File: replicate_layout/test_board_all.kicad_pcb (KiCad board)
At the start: 2 copper layers, 30 parts, among them J1001 Pusa_4mm, J1002 Pusa_4mm, Q1001 CSD19531KCS, Q1002 CSD19531KCS, Q1003 CSD19531KCS, Q2001 CSD19531KCS, Q2002 CSD19531KCS, Q3001 CSD19531KCS, Q3002 CSD19531KCS, Q4001 CSD19531KCS, Q4002 CSD19531KCS, U1001 LAUNCHXL-F28377S, U2001 IR2181, U3001 IR2181, U4001 IR2181

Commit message: polarna replikacija dela GUI še ne dela samo še zone je treba replicirati
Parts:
- moved Q1001 147.0 mm to (40.6, 167.6)
- moved Q1002 147.0 mm to (29.8, 175.3)
- moved Q1003 147.0 mm to (29.2, 188.6)
- moved U1001 61.4 mm to (19.7, 48.9)
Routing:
- net /Veja_3/OUT: track 63.8 -> 44.0 mm
- removed copper zone on F.Cu, net /Veja_1/OUT
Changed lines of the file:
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@@
     (thickness 1.6)
     (drawings 0)
-    (tracks 149)
+    (tracks 146)
     (zones 0)
     (modules 30)
@@
     (tags "capacitor 1206")
     (attr smd)
-    (fp_text reference C2001 (at 0 -1.75) (layer F.SilkS)
+    (fp_text reference C2001 (at 4.675 0) (layer F.SilkS)
       (effects (font (size 1 1) (thickness 0.15)))
     )
@@
     (tags "capacitor 1206")
     (attr smd)
-    (fp_text reference C3001 (at 0 -1.75) (layer F.SilkS)
+    (fp_text reference C3001 (at 4.675 0) (layer F.SilkS)
       (effects (font (size 1 1) (thickness 0.15)))
     )
@@
     (tags "capacitor 1206")
     (attr smd)
-    (fp_text reference C4001 (at 0 -1.75) (layer F.SilkS)
+    (fp_text reference C4001 (at 4.675 0) (layer F.SilkS)
       (effects (font (size 1 1) (thickness 0.15)))
     )
@@
     (tags "Diode Mini-MELF")
     (attr smd)
-    (fp_text reference D2001 (at 0 -2 270) (layer F.SilkS)
+    (fp_text reference D2001 (at 0 1.905 270) (layer F.SilkS)
       (effects (font (size 1 1) (thickness 0.15)))
     )
@@
       (effects (font (size 1 1) (thickness 0.15)))
     )
-    (fp_text user %R (at 0 -2 270) (layer F.Fab)
+    (fp_text user %R (at 0 1.905 270) (layer F.Fab)
       (effects (font (size 1 1) (thickness 0.15)))
     )
@@
     (tags "Diode Mini-MELF")
     (attr smd)
-    (fp_text reference D3001 (at 0 -2 270) (layer F.SilkS)
+    (fp_text reference D3001 (at 0 1.905 270) (layer F.SilkS)
       (effects (font (size 1 1) (thickness 0.15)))
     )
@@
       (effects (font (size 1 1) (thickness 0.15)))
     )
-    (fp_text user %R (at 0 -2 270) (layer F.Fab)
+    (fp_text user %R (at 0 1.905 270) (layer F.Fab)
       (effects (font (size 1 1) (thickness 0.15)))
     )
@@
     (tags "Diode Mini-MELF")
     (attr smd)
-    (fp_text reference D4001 (at 0 -2 270) (layer F.SilkS)
+    (fp_text reference D4001 (at 0 1.905 270) (layer F.SilkS)
       (effects (font (size 1 1) (thickness 0.15)))
     )
@@
       (effects (font (size 1 1) (thickness 0.15)))
     )
-    (fp_text user %R (at 0 -2 270) (layer F.Fab)
+    (fp_text user %R (at 0 1.905 270) (layer F.Fab)
       (effects (font (size 1 1) (thickness 0.15)))
     )
@@
   )
   (module Discretes:TO-220 (layer F.Cu)
-    (at 182.245 128.27)
+    (at 40.64 167.64)
     (descr "TO-220-3, Vertical, RM 2.54mm")
     (tags "TO-220-3 Vertical RM 2.54mm")
@@
   )
   (module Discretes:TO-220 (layer F.Cu)
-    (at 171.45 135.89)
+    (at 29.845 175.26)
     (descr "TO-220-3, Vertical, RM 2.54mm")
     (tags "TO-220-3 Vertical RM 2.54mm")
@@
   )
   (module Discretes:TO-220 (layer F.Cu)
-    (at 170.815 149.225)
+    (at 29.21 188.595)
     (descr "TO-220-3, Vertical, RM 2.54mm")
     (tags "TO-220-3 Vertical RM 2.54mm")
@@
   )
   (module TI_modules:28379D_launchpad (layer F.Cu)
-    (at 75.565 74.295 270)
+    (at 19.685 48.895 270)
     (descr "28379D launchpad")
     (tags DEV)
@@
     (tags "SOIC 1.27")
     (attr smd)
-    (fp_text reference U2001 (at 0 -3.5 90) (layer F.SilkS)
+    (fp_text reference U2001 (at -5.08 -3.81 90) (layer F.SilkS)
       (effects (font (size 1 1) (thickness 0.15)))
     )
@@
     (tags "SOIC 1.27")
     (attr smd)
-    (fp_text reference U3001 (at 0 -3.5 90) (layer F.SilkS)
+    (fp_text reference U3001 (at -5.08 -3.81 90) (layer F.SilkS)
       (effects (font (size 1 1) (thickness 0.15)))
     )
@@
     (tags "SOIC 1.27")
     (attr smd)
-    (fp_text reference U4001 (at 0 -3.5 90) (layer F.SilkS)
+    (fp_text reference U4001 (at -5.08 -3.81 90) (layer F.SilkS)
       (effects (font (size 1 1) (thickness 0.15)))
     )
@@
   (segment (start 200.66 106.235) (end 201.105 106.68) (width 0.5) (layer F.Cu) (net 1))
   (segment (start 200.66 102.715) (end 200.66 106.235) (width 0.5) (layer F.Cu) (net 1))
-  (segment (start 229.87 91.44) (end 229.87 92.075) (width 2) (layer F.Cu) (net 13))
-  (segment (start 234.95 86.36) (end 229.87 91.44) (width 2) (layer F.Cu) (net 13))
-  (segment (start 247.015 86.36) (end 234.95 86.36) (width 2) (layer F.Cu) (net 13))
   (segment (start 177.8 102.715) (end 177.8 106.235) (width 0.5) (layer F.Cu) (net 1))
   (segment (start 177.8 106.235) (end 178.245 106.68) (width 0.5) (layer F.Cu) (net 1))
@@
   (segment (start 186.69 101.29) (end 184.315 103.665) (width 0.5) (layer F.Cu) (net 25))
   (segment (start 184.315 103.665) (end 183.515 103.665) (width 0.5) (layer F.Cu) (net 25))
-  (zone (net 3) (net_name /Veja_1/OUT) (layer F.Cu) (hatch edge 0.508)
+  (zone (net 4) (net_name /Veja_2/OUT) (layer F.Cu) (hatch edge 0.508)
     (connect_pads (clearance 0.508))
     (min_thickness 0.254)
-    (fill yes (arc_segments 16) (thermal_gap 0.508) (thermal_bridge_width 0.508))
+    (fill (arc_segments 16) (thermal_gap 0.508) (thermal_bridge_width 0.508))
     (polygon
       (pts
-        (xy 181.61 86.995) (xy 184.15 86.995) (xy 184.15 93.345) (xy 181.61 93.345)
+        (xy 204.47 86.995) (xy 207.01 86.995) (xy 207.01 93.345) (xy 204.47 93.345)
       )
     )
@@
       )
     )
-  )
-  (zone (net 4) (net_name /Veja_2/OUT) (layer F.Cu) (hatch edge 0.508)
-    (connect_pads (clearance 0.508))
-    (min_thickness 0.254)
-    (fill (arc_segments 16) (thermal_gap 0.508) (thermal_bridge_width 0.508))
-    (polygon
-      (pts
-        (xy 204.47 86.995) (xy 207.01 86.995) (xy 207.01 93.345) (xy 204.47 93.345)
-      )
-    )
-  )
-  (zone (net 2) (net_name GND) (layer F.Cu) (hatch edge 0.508)
-    (connect_pads (clearance 0.508))
-    (min_thickness 0.254)
-    (fill yes (arc_segments 16) (thermal_gap 0.508) (thermal_bridge_width 0.508))
-    (polygon
-      (pts
-        (xy 188.595 92.075) (xy 188.595 90.17) (xy 191.77 90.17) (xy 191.77 92.075)
-      )
-    )
-  )
-  (zone (net 3) (net_name /Veja_1/OUT) (layer F.Cu) (hatch edge 0.508)
-    (connect_pads (clearance 0.508))
-    (min_thickness 0.254)
-    (fill yes (arc_segments 16) (thermal_gap 0.508) (thermal_bridge_width 0.508))
-    (polygon
-      (pts
-        (xy 182.88 77.47) (xy 182.88 85.09) (xy 191.135 85.09) (xy 191.135 77.47)
-      )
-    )

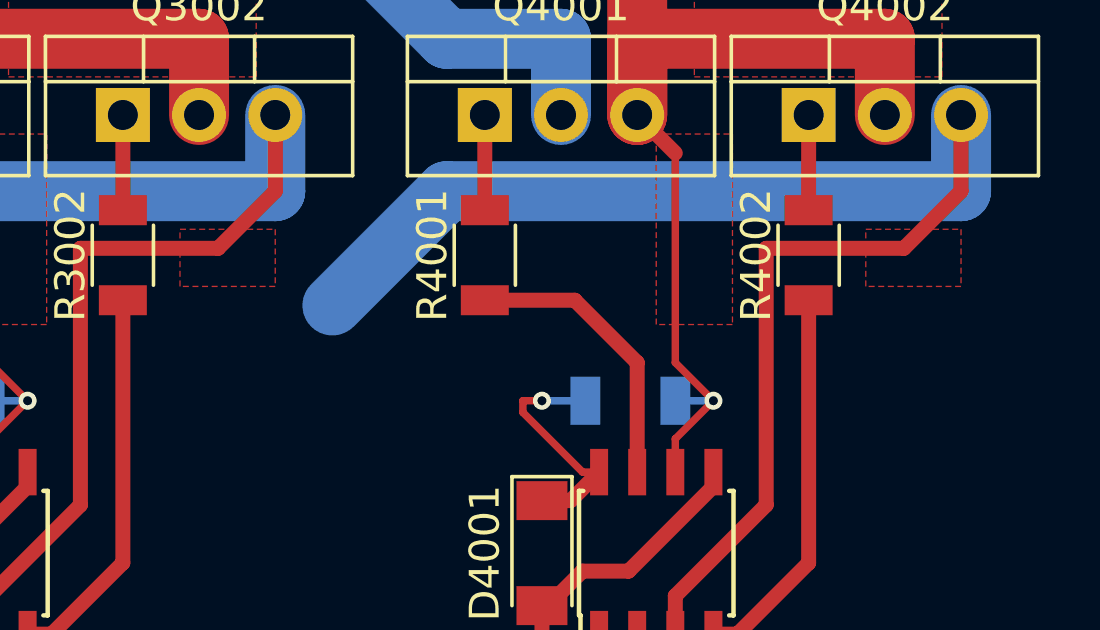
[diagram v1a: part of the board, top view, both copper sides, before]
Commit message: fixed a bug in test function changed how bounding box is calculated
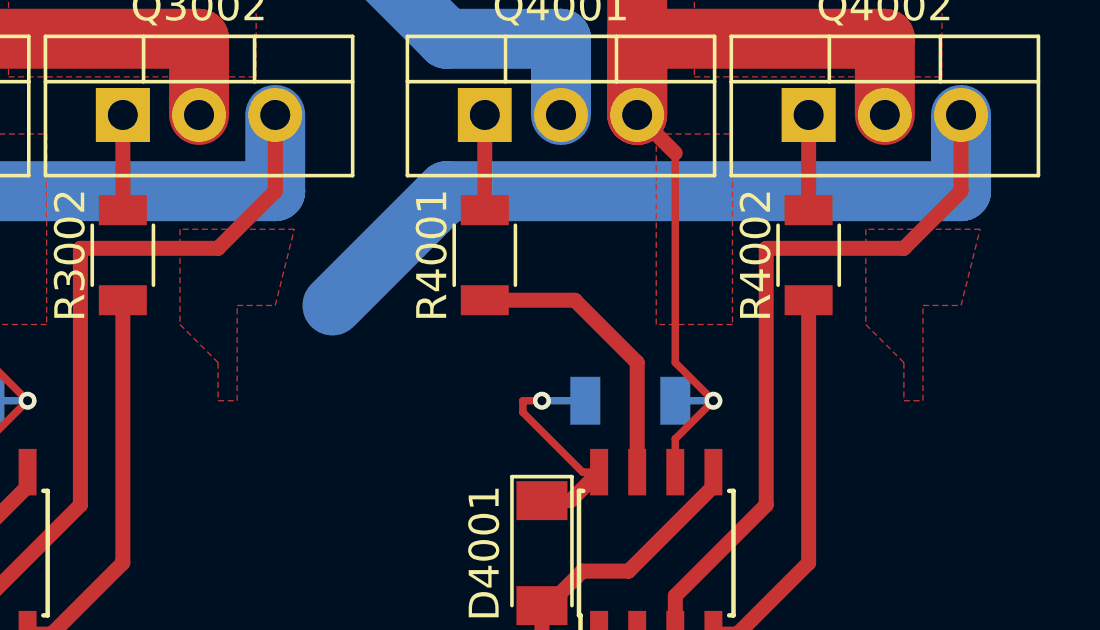
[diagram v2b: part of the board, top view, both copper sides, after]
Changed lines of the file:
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@@
+    )
+  )
+  (zone (net 2) (net_name GND) (layer F.Cu) (hatch edge 0.508)
+    (connect_pads (clearance 0.508))
+    (min_thickness 0.254)
+    (fill (arc_segments 16) (thermal_gap 0.508) (thermal_bridge_width 0.508))
+    (polygon
+      (pts
+        (xy 234.315 90.17) (xy 234.315 93.345) (xy 235.585 94.615) (xy 235.585 95.885) (xy 236.22 95.885)
+        (xy 236.22 92.71) (xy 237.49 92.71) (xy 238.125 90.17)
+      )
     )
   )
@@
       (pts
         (xy 228.6 77.47) (xy 228.6 85.09) (xy 236.855 85.09) (xy 236.855 77.47)
-      )
-    )
-  )
-  (zone (net 2) (net_name GND) (layer F.Cu) (hatch edge 0.508)
-    (connect_pads (clearance 0.508))
-    (min_thickness 0.254)
-    (fill (arc_segments 16) (thermal_gap 0.508) (thermal_bridge_width 0.508))
-    (polygon
-      (pts
-        (xy 234.315 92.075) (xy 234.315 90.17) (xy 237.49 90.17) (xy 237.49 92.075)
       )
     )
@@
     )
   )
+  (zone (net 2) (net_name GND) (layer F.Cu) (hatch edge 0.508)
+    (connect_pads (clearance 0.508))
+    (min_thickness 0.254)
+    (fill (arc_segments 16) (thermal_gap 0.508) (thermal_bridge_width 0.508))
+    (polygon
+      (pts
+        (xy 211.455 90.17) (xy 211.455 93.345) (xy 212.725 94.615) (xy 212.725 95.885) (xy 213.36 95.885)
+        (xy 213.36 92.71) (xy 214.63 92.71) (xy 215.265 90.17)
+      )
+    )
+  )
   (zone (net 4) (net_name /Veja_2/OUT) (layer F.Cu) (hatch edge 0.508)
     (connect_pads (clearance 0.508))
@@
       )
     )
-  )
-  (zone (net 2) (net_name GND) (layer F.Cu) (hatch edge 0.508)
-    (connect_pads (clearance 0.508))
-    (min_thickness 0.254)
-    (fill (arc_segments 16) (thermal_gap 0.508) (thermal_bridge_width 0.508))
-    (polygon
-      (pts
-        (xy 211.455 92.075) (xy 211.455 90.17) (xy 214.63 90.17) (xy 214.63 92.075)
-      )
-    )

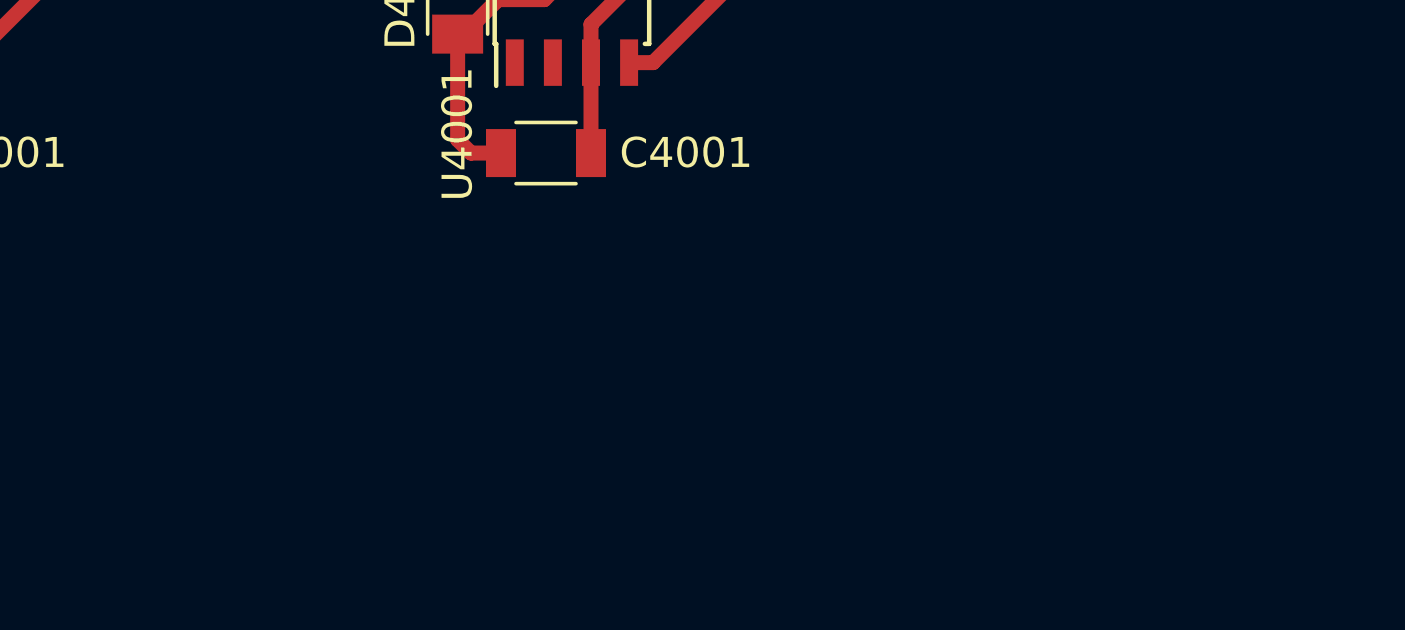
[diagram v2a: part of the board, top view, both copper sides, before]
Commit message: Pre-fill minimum replication steps. Modifed test cases
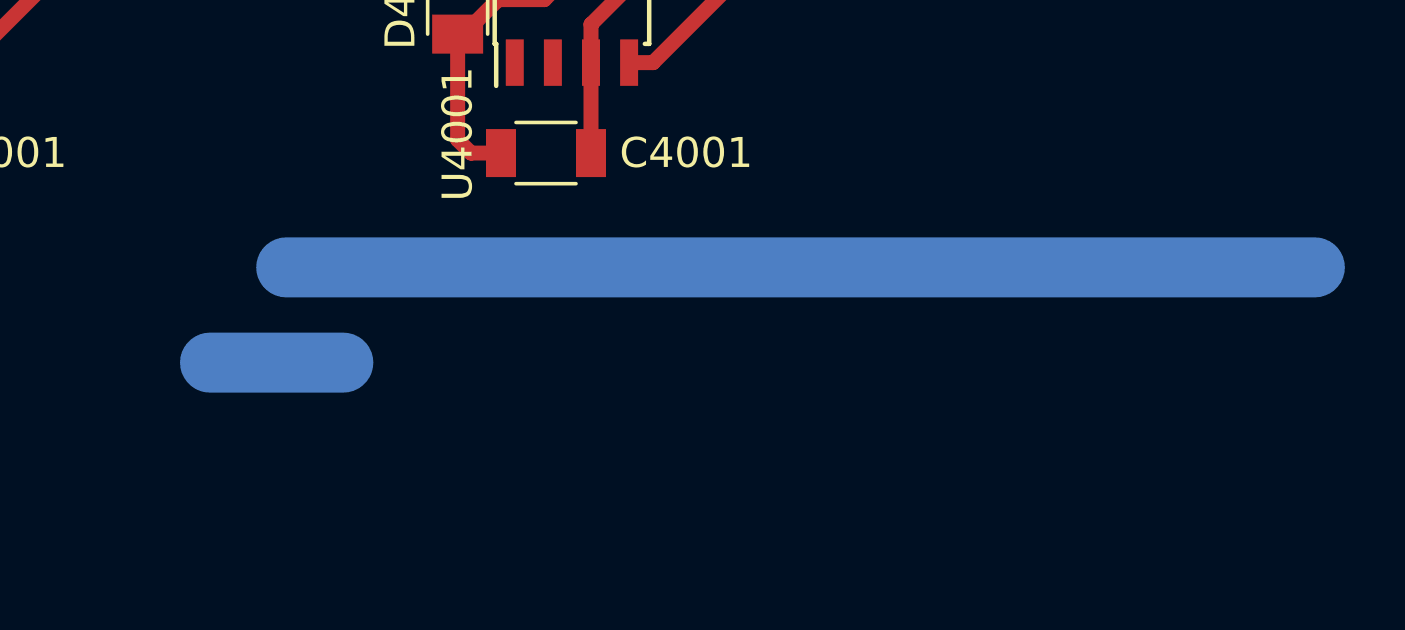
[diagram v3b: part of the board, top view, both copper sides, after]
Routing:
- net (no net): track 0.00 -> 38.7 mm

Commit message: Updated documentation
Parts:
- moved C4001 4.28 mm to (230.7, 106.7)
- moved C4002 4.28 mm to (230.7, 95.9)
- moved D4001 4.28 mm to (227.8, 101.0)
- moved Q4001 4.28 mm to (225.9, 86.4)
- moved Q4002 4.28 mm to (236.7, 86.4)
- moved R4001 4.28 mm to (225.9, 91.0)
- moved R4002 4.28 mm to (236.7, 91.0)
- moved U4001 4.28 mm to (231.6, 101.0)
- moved C3001 2.14 mm to (205.7, 106.7)
- moved C3002 2.14 mm to (205.7, 95.9)
- moved D3001 2.14 mm to (202.8, 101.0)
- moved Q3001 2.14 mm to (200.9, 86.4)
- moved R3001 2.14 mm to (200.9, 91.0)
- moved U3001 2.14 mm to (206.6, 101.0)
- moved Q3002 2.14 mm to (211.7, 86.4)
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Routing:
- added copper zone on F.Cu, net /Veja_1/OUT

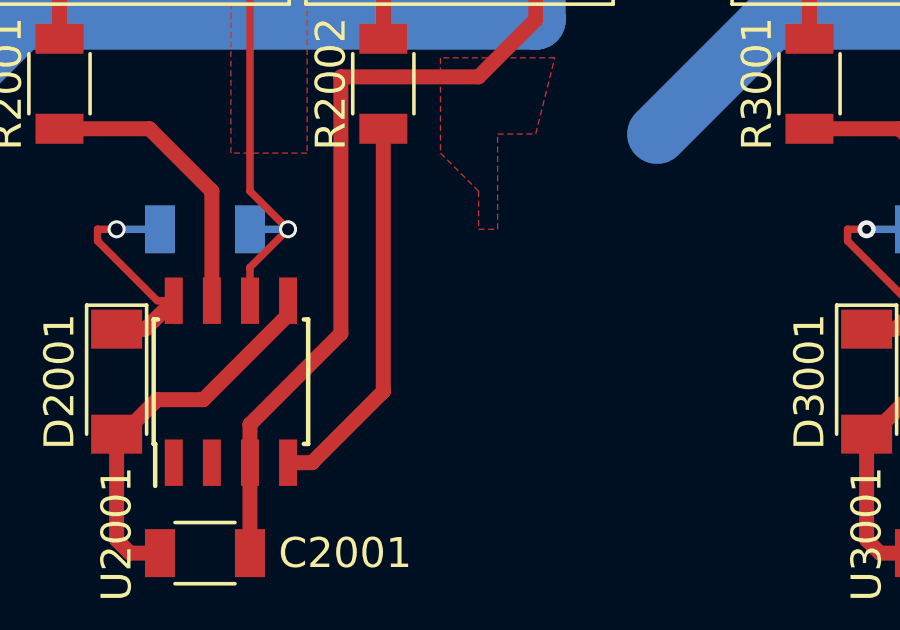
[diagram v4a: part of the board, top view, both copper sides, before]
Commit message: Bugfix for circular module orientation in linear replication
Updated test layouts as it tests for non copper zones also
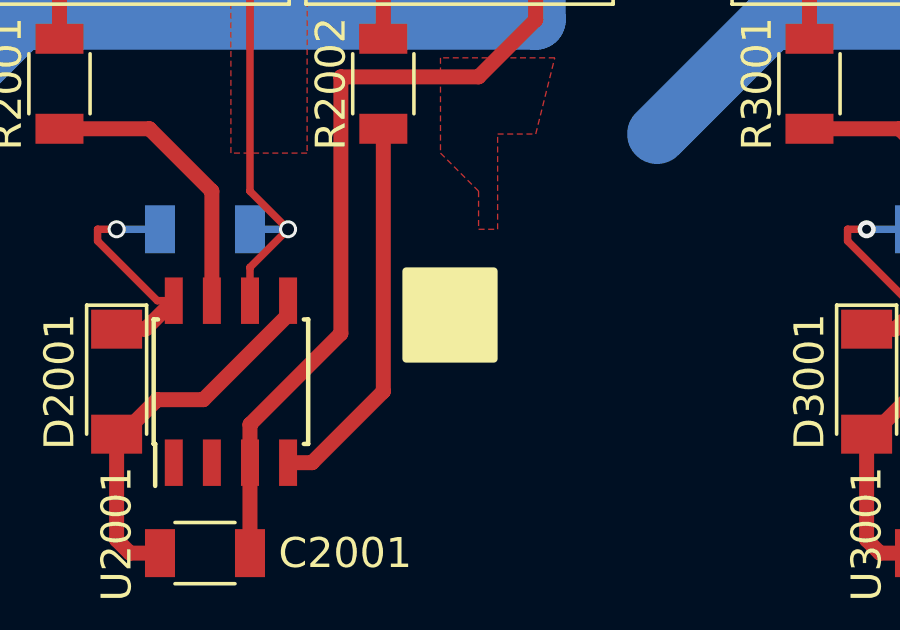
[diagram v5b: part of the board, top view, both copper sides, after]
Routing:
- net +VDC: track 39.8 -> 78.5 mm
- net (no net): track 38.7 -> 0.00 mm
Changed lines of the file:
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@@
   (segment (start 202.8 106.235) (end 203.245 106.68) (width 0.5) (layer F.Cu) (net 1))
   (segment (start 202.8 102.715) (end 202.8 106.235) (width 0.5) (layer F.Cu) (net 1))
-  (segment (start 215.265 113.665) (end 219.71 113.665) (width 2) (layer B.Cu) (net 0))
-  (segment (start 217.805 110.49) (end 252.095 110.49) (width 2) (layer B.Cu) (net 0))
+  (segment (start 215.265 113.665) (end 219.71 113.665) (width 2) (layer B.Cu) (net 5))
+  (segment (start 217.805 110.49) (end 252.095 110.49) (width 2) (layer B.Cu) (net 5))
   (segment (start 177.8 102.715) (end 177.8 106.235) (width 0.5) (layer F.Cu) (net 1))
   (segment (start 177.8 106.235) (end 178.245 106.68) (width 0.5) (layer F.Cu) (net 1))
@@
     )
   )
+  (zone (net 0) (net_name "") (layer F.SilkS) (hatch edge 0.508)
+    (connect_pads (clearance 0.508))
+    (min_thickness 0.254)
+    (fill (arc_segments 16) (thermal_gap 0.508) (thermal_bridge_width 0.508))
+    (polygon
+      (pts
+        (xy 237.325 97.155) (xy 240.5 97.155) (xy 240.5 100.33) (xy 237.325 100.33)
+      )
+    )
+  )
   (zone (net 13) (net_name /Veja_3/OUT) (layer F.Cu) (hatch edge 0.508)
     (connect_pads (clearance 0.508))
@@
         (xy 238.595 90.17) (xy 238.595 93.345) (xy 239.865 94.615) (xy 239.865 95.885) (xy 240.5 95.885)
         (xy 240.5 92.71) (xy 241.77 92.71) (xy 242.405 90.17)
+      )
+    )
+  )
+  (zone (net 0) (net_name "") (layer F.SilkS) (hatch edge 0.508)
+    (connect_pads (clearance 0.508))
+    (min_thickness 0.254)
+    (fill (arc_segments 16) (thermal_gap 0.508) (thermal_bridge_width 0.508))
+    (polygon
+      (pts
+        (xy 212.325 97.155) (xy 215.5 97.155) (xy 215.5 100.33) (xy 212.325 100.33)
       )
     )
@@
       )
     )
+  )
+  (zone (net 0) (net_name "") (layer F.SilkS) (hatch edge 0.508)
+    (connect_pads (clearance 0.508))
+    (min_thickness 0.254)
+    (fill yes (arc_segments 16) (thermal_gap 0.508) (thermal_bridge_width 0.508))
+    (polygon
+      (pts
+        (xy 187.325 97.155) (xy 190.5 97.155) (xy 190.5 100.33) (xy 187.325 100.33)
+      )
+    )
